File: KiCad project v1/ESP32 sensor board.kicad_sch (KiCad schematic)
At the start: 33 parts, among them J1 USB_C_Receptacle, J3 JST_2mm_LiPo, U1 MCP73871, U2 AMS1117-3.3

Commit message: Small fixes.
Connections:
- net at J1.A8 (NC): no longer J1.B8 (NC)
- net at J1.NC2 (NC), J1.NC3 (NC): no longer J1.NC1 (NC)
- net D+ renamed USB_DN
- net D- renamed USB_DP
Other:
- sheet ESP32-C3-02 ports: added USB_DN, USB_DP; removed D+, D-
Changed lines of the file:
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@@
 	)
 	(junction
-		(at 30.48 95.25)
+		(at 30.48 94.9325)
 		(diameter 0)
 		(color 0 0 0 0)
@@
 	(wire
 		(pts
-			(xy 203.2 49.53) (xy 203.2 53.34)
+			(xy 63.5 155.2575) (xy 67.31 155.2575)
 		)
 		(stroke
@@
 	(wire
 		(pts
-			(xy 63.5 160.02) (xy 67.31 160.02)
+			(xy 203.2 49.53) (xy 203.2 53.34)
 		)
 		(stroke
@@
 	(wire
 		(pts
+			(xy 30.48 94.9325) (xy 30.48 101.6)
+		)
+		(stroke
+			(width 0)
+			(type default)
+		)
+	)
+	(wire
+		(pts
 			(xy 139.7 49.53) (xy 127 49.53)
 		)
@@
 	(wire
 		(pts
+			(xy 63.5 160.02) (xy 67.31 160.02)
+		)
+		(stroke
+			(width 0)
+			(type default)
+		)
+	)
+	(wire
+		(pts
 			(xy 231.14 102.87) (xy 231.14 109.22)
 		)
@@
 	(wire
 		(pts
+			(xy 22.86 91.44) (xy 22.86 94.9325)
+		)
+		(stroke
+			(width 0)
+			(type default)
+		)
+	)
+	(wire
+		(pts
 			(xy 233.68 60.96) (xy 267.97 60.96)
 		)
@@
 	(wire
 		(pts
-			(xy 30.48 95.25) (xy 30.48 101.6)
+			(xy 30.48 91.44) (xy 30.48 94.9325)
 		)
 		(stroke
@@
 	(wire
 		(pts
-			(xy 63.5 156.21) (xy 67.31 156.21)
-		)
-		(stroke
-			(width 0)
-			(type default)
-		)
-	)
-	(wire
-		(pts
 			(xy 110.49 76.2) (xy 115.57 76.2)
 		)
@@
 	(wire
 		(pts
+			(xy 22.86 94.9325) (xy 30.48 94.9325)
+		)
+		(stroke
+			(width 0)
+			(type default)
+		)
+	)
+	(wire
+		(pts
 			(xy 185.42 63.5) (xy 175.26 63.5)
 		)
@@
 	(wire
 		(pts
-			(xy 22.86 95.25) (xy 30.48 95.25)
-		)
-		(stroke
-			(width 0)
-			(type default)
-		)
-	)
-	(wire
-		(pts
 			(xy 220.98 86.36) (xy 231.14 86.36)
 		)
@@
 	(wire
 		(pts
-			(xy 30.48 91.44) (xy 30.48 95.25)
+			(xy 45.72 82.55) (xy 52.07 82.55)
 		)
 		(stroke
@@
 	(wire
 		(pts
-			(xy 45.72 82.55) (xy 52.07 82.55)
+			(xy 233.68 66.04) (xy 250.19 66.04)
 		)
 		(stroke
@@
 		)
 	)
-	(wire
-		(pts
-			(xy 22.86 91.44) (xy 22.86 95.25)
-		)
+	(text_box "See ESP32 S3 Dev Kit reference design:\nhttps://txplo.re/esp32s3ref"
+		(exclude_from_sim no)
+		(at 86.6775 181.9275 0)
+		(size 43.815 7.3025)
 		(stroke
 			(width 0)
 			(type default)
 		)
-	)
-	(wire
-		(pts
-			(xy 233.68 66.04) (xy 250.19 66.04)
+		(fill
+			(type none)
 		)
-		(stroke
-			(width 0)
-			(type default)
+		(effects
+			(font
+				(size 1.27 1.27)
+			)
+			(justify left top)
 		)
 	)
@@
 		)
 	)
-	(label "D+"
+	(label "USB_DP"
 		(at 67.31 160.02 0)
 		(fields_autoplaced yes)
@@
 		)
 	)
-	(label "D-"
-		(at 67.31 156.21 0)
+	(label "USB_DN"
+		(at 67.31 155.2575 0)
 		(fields_autoplaced yes)
 		(effects
@@
 		)
 	)
-	(label "D+"
+	(label "USB_DN"
 		(at 45.72 71.12 0)
 		(fields_autoplaced yes)
@@
 		)
 	)
-	(label "D-"
+	(label "USB_DP"
 		(at 45.72 73.66 0)
 		(fields_autoplaced yes)
@@
 			)
 		)
+		(property "Instructions and notes" ""
+			(at 30.48 71.12 0)
+			(effects
+				(font
+					(size 1.27 1.27)
+				)
+				(hide yes)
+			)
+		)
+		(property "Field-1" ""
+			(at 30.48 71.12 0)
+			(effects
+				(font
+					(size 1.27 1.27)
+				)
+				(hide yes)
+			)
+		)
 		(pin "B7"
 		)
@@
 			)
 		)
-		(pin "D-" input
-			(at 63.5 156.21 0)
+		(pin "USB_DP" input
+			(at 63.5 160.02 0)
 			(effects
 				(font
@@
 			)
 		)
-		(pin "D+" input
-			(at 63.5 160.02 0)
+		(pin "USB_DN" input
+			(at 63.5 155.2575 0)
 			(effects
 				(font

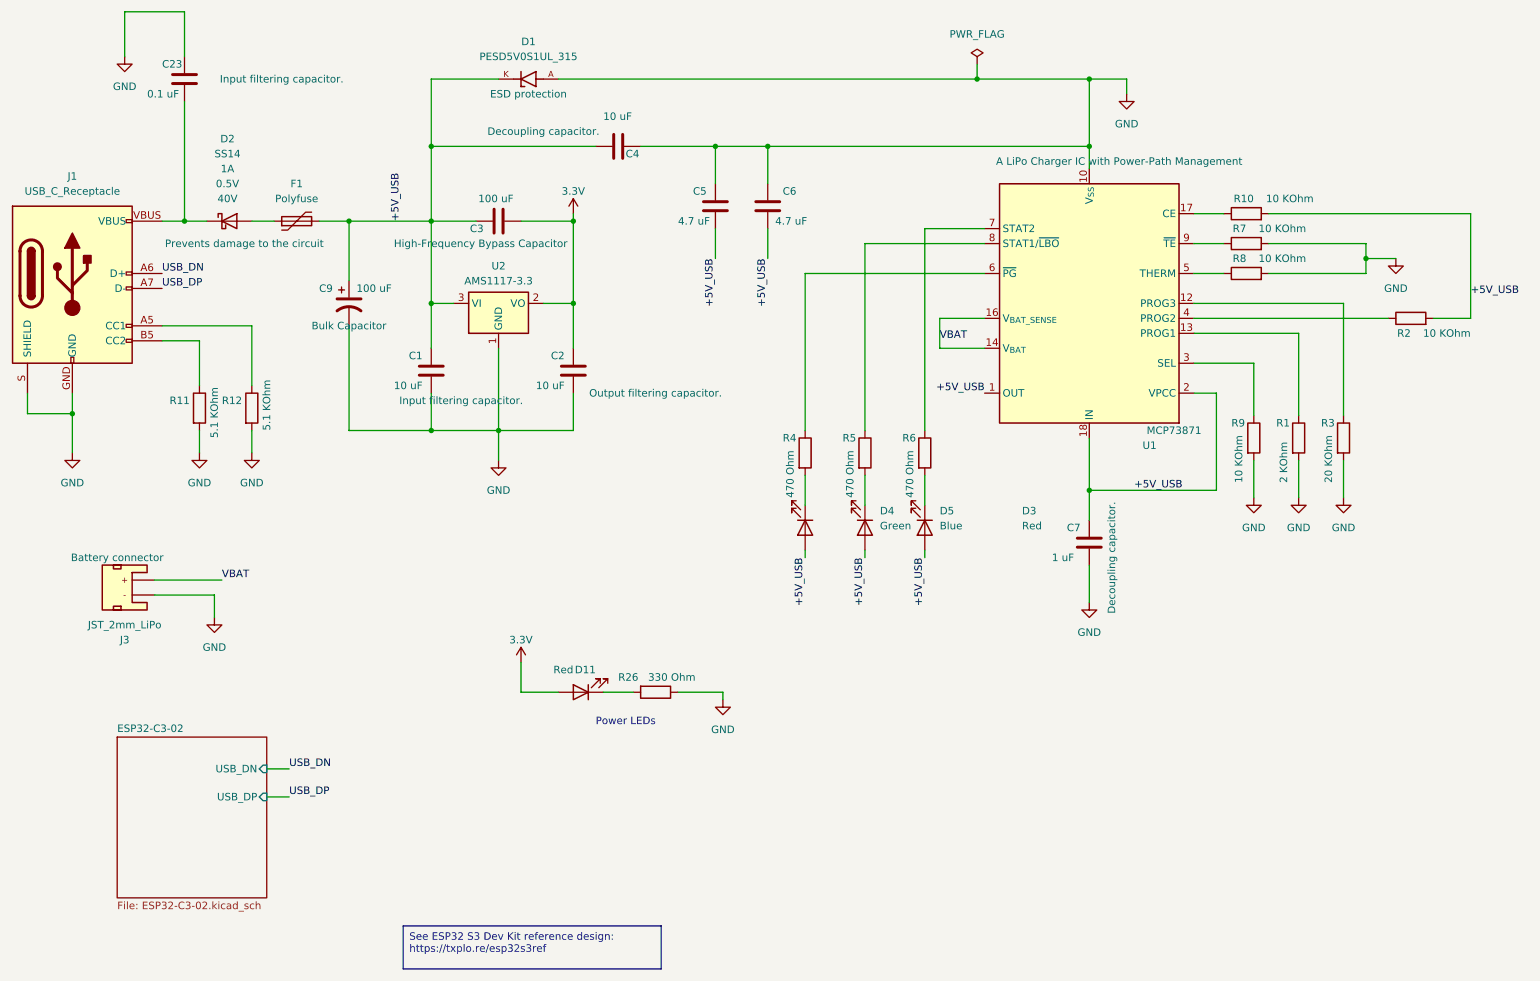
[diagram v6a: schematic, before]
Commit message: Simplifying component values by removing units.
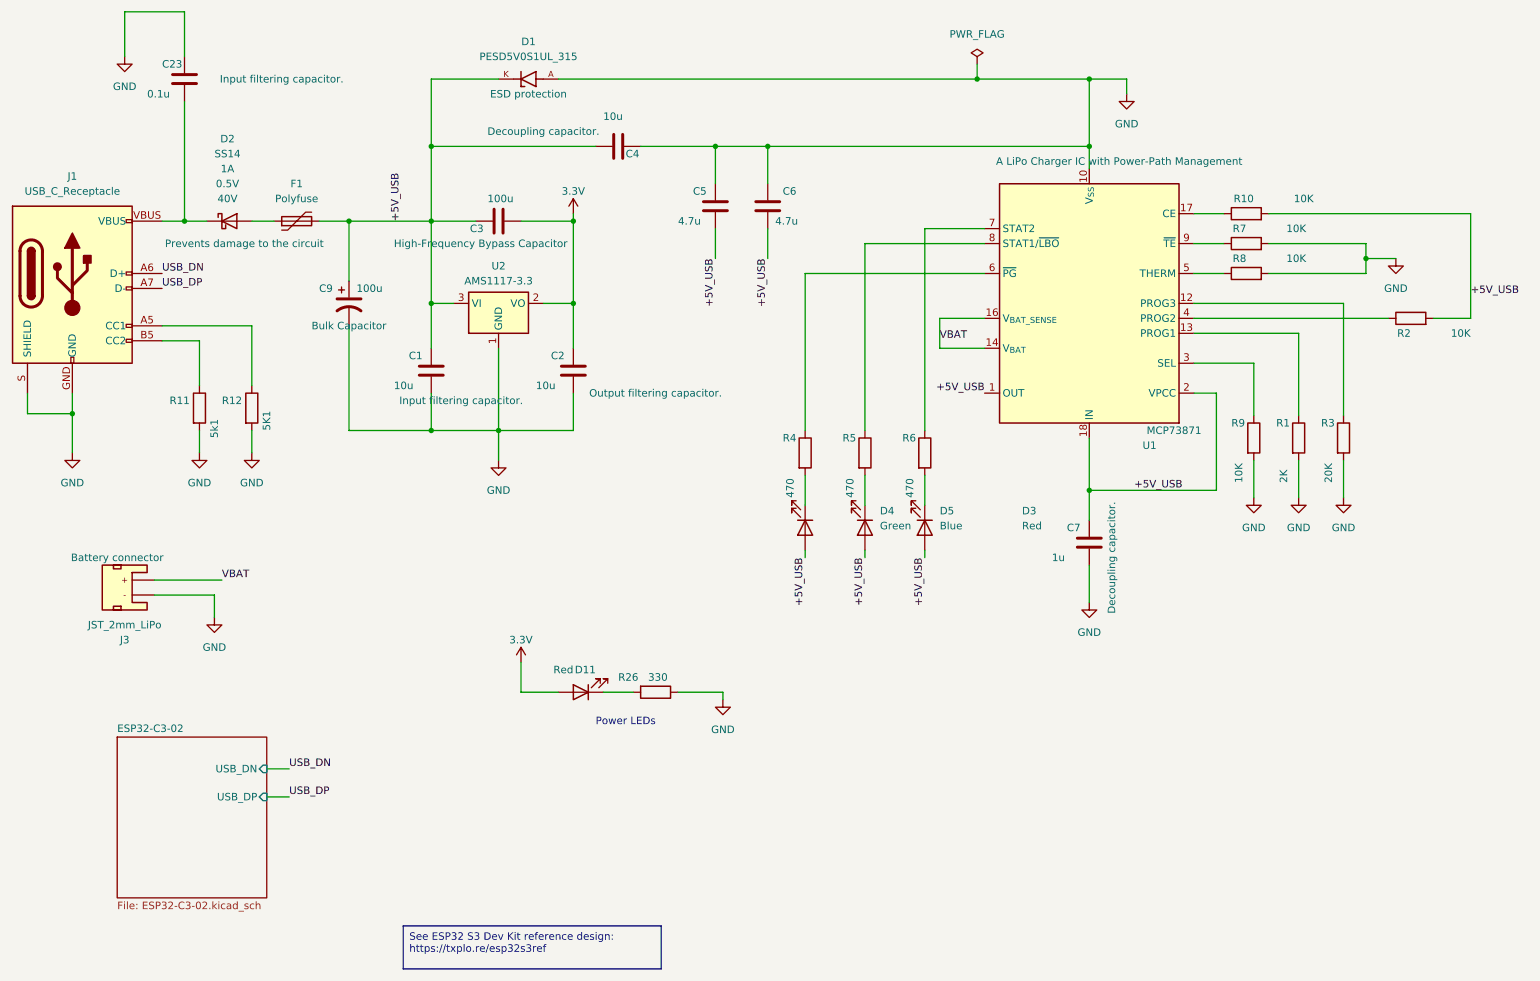
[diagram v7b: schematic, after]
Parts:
- C1, C2, C4: value 10 uF -> 10u
- C23: value 0.1 uF -> 0.1u
- C3, C9: value 100 uF -> 100u
- C5, C6: value 4.7 uF -> 4.7u
- C7: value 1 uF -> 1u
- R1: value 2 KOhm -> 2K
- R10, R2, R7, R8, R9: value 10 KOhm -> 10K
- R11: value 5.1 KOhm -> 5k1
- R12: value 5.1 KOhm -> 5K1
- R26: value 330 Ohm -> 330
- R3: value 20 KOhm -> 20K
- R4, R5, R6: value 470 Ohm -> 470
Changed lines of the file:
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@@
 			)
 		)
-		(property "Value" "10 uF"
+		(property "Value" "10u"
 			(at 109.22 90.17 0)
 			(effects
@@
 			)
 		)
-		(property "Value" "2 KOhm"
+		(property "Value" "2K"
 			(at 236.22 106.68 90)
 			(effects
@@
 			)
 		)
-		(property "Value" "10 KOhm"
+		(property "Value" "10K"
 			(at 228.6 106.68 90)
 			(effects
@@
 			)
 		)
-		(property "Value" "10 KOhm"
+		(property "Value" "10K"
 			(at 240.03 68.58 90)
 			(effects
@@
 			)
 		)
-		(property "Value" "470 Ohm"
+		(property "Value" "470"
 			(at 152.4 109.22 90)
 			(effects
@@
 			)
 		)
-		(property "Value" "4.7 uF"
+		(property "Value" "4.7u"
 			(at 149.86 62.23 0)
 			(effects
@@
 			)
 		)
-		(property "Value" "10 KOhm"
+		(property "Value" "10K"
 			(at 267.97 81.28 90)
 			(effects
@@
 			)
 		)
-		(property "Value" "100 uF"
+		(property "Value" "100u"
 			(at 105.41 58.42 90)
 			(effects
@@
 			)
 		)
-		(property "Value" "4.7 uF"
+		(property "Value" "4.7u"
 			(at 133.35 62.23 0)
 			(effects
@@
 			)
 		)
-		(property "Value" "5.1 KOhm"
+		(property "Value" "5k1"
 			(at 54.61 99.06 90)
 			(effects
@@
 			)
 		)
-		(property "Value" "10 KOhm"
+		(property "Value" "10K"
 			(at 241.3 58.42 90)
 			(effects
@@
 			)
 		)
-		(property "Value" "330 Ohm"
+		(property "Value" "330"
 			(at 128.27 139.7 90)
 			(effects
@@
 			)
 		)
-		(property "Value" "10 uF"
+		(property "Value" "10u"
 			(at 85.09 90.17 0)
 			(effects
@@
 			)
 		)
-		(property "Value" "470 Ohm"
+		(property "Value" "470"
 			(at 162.56 109.22 90)
 			(effects
@@
 			)
 		)
-		(property "Value" "10 uF"
+		(property "Value" "10u"
 			(at 120.65 44.45 90)
 			(effects
@@
 			)
 		)
-		(property "Value" "20 KOhm"
+		(property "Value" "20K"
 			(at 243.84 106.68 90)
 			(effects
@@
 			)
 		)
-		(property "Value" "5.1 KOhm"
+		(property "Value" "5K1"
 			(at 63.5 97.79 90)
 			(effects
@@
 			)
 		)
-		(property "Value" "10 KOhm"
+		(property "Value" "10K"
 			(at 240.03 63.5 90)
 			(effects
@@
 			)
 		)
-		(property "Value" "100 uF"
+		(property "Value" "100u"
 			(at 78.74 73.66 0)
 			(effects
@@
 			)
 		)
-		(property "Value" "1 uF"
+		(property "Value" "1u"
 			(at 196.85 119.38 0)
 			(effects
@@
 			)
 		)
-		(property "Value" "0.1 uF"
+		(property "Value" "0.1u"
 			(at 43.18 40.64 0)
 			(effects
@@
 			)
 		)
-		(property "Value" "470 Ohm"
+		(property "Value" "470"
 			(at 172.72 109.22 90)
 			(effects
